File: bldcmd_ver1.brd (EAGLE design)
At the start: 43 x 49 mm, 94 parts, among them CN1 DF61-2P-2.2V(23), CN2 DF65-3P-1.7V(21), CN3 SM05B-SRSS-TB, CN5 SM04B-SRSS-TB, CN6 SM05B-SRSS-TB, CN7 SM04B-SRSS-TB, IC1 STSPIN32F0A, IC2 AS5047P-ATSM, IC3 ADM4852ACPZ-REEL7, Q1 PSMN2R4-30MLD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

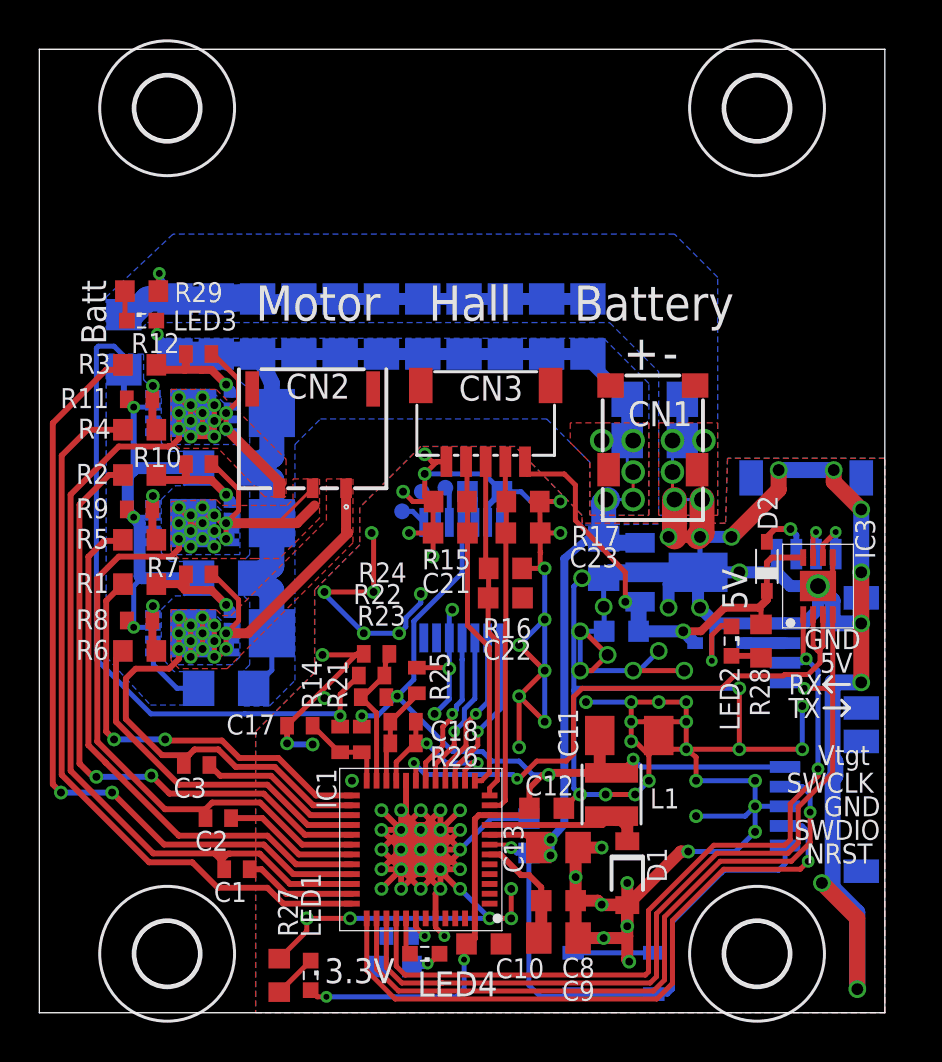
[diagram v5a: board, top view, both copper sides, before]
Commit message: RS485のICをSOIC8のものに変更
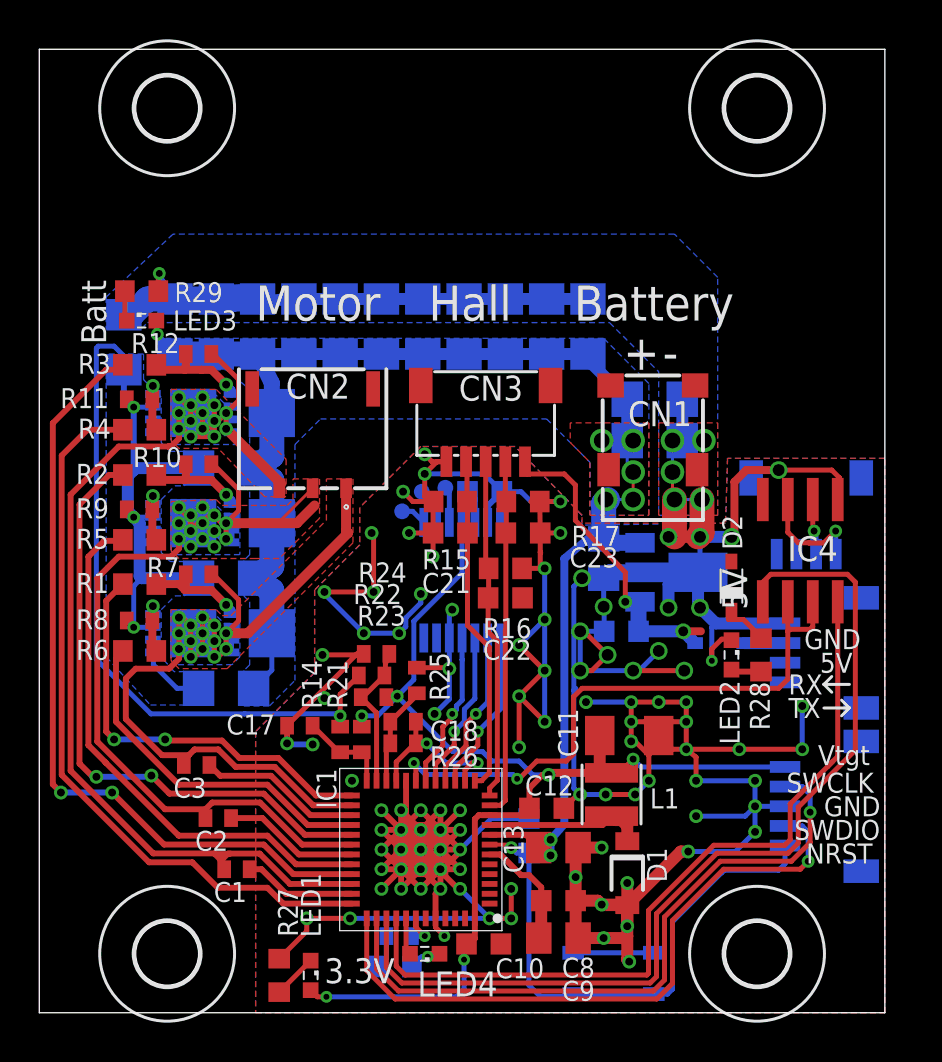
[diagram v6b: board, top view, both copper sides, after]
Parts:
- removed IC3: ADM4852ACPZ-REEL7, rcssl_lib:SON50P300X300X85-9N
- added IC4: LTC485S, linear-technology:SOIC8
- moved D2 2.06 mm to (35.2, 21.7)
- moved LED2 0.70 mm to (35.2, 18.2)
- moved R28 0.70 mm to (36.7, 18.2)
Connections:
- net +5V: now also IC4.8; no longer IC3.8
- net GND: now also IC4.5; no longer IC3.5, IC3.9
- net N$29: now also IC4.6; no longer IC3.7
- net N$32: now also IC4.7; no longer IC3.6
- net RTS: now also IC4.2, IC4.3; no longer IC3.2, IC3.3
- net UART_RX: now also IC1.39, IC4.1; no longer CN5.3, IC1.40, IC3.1
- net UART_TX: now also IC1.40, IC4.4; no longer CN5.4, IC1.39, IC3.4
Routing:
- net GND: track 382.9 -> 322.3 mm, vias 118 -> 108
- net UART_RX: track 40.8 -> 49.1 mm, vias 2 -> 0
- net +5V: track 25.9 -> 19.2 mm
- net UART_TX: track 44.3 -> 40.8 mm, vias 1 -> 0
- net N$32: track 2.69 -> 5.75 mm
- net N$30: track 3.01 -> 0.00 mm, vias 1 -> 0

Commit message: AW進捗
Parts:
- removed CN3: SM05B-SRSS-TB, scramble-con-jst:SM05B-SRSS-TB
- added CN4: DF57H-5P-1.2V(21), scramble-con-hirose:DF57H-5P-1.2V(21)
- C21, C22, C23: device rcl:C0603K -> rcl:C0402
- R15, R16, R17: device rcl:R0603 -> rcl:R0402
- moved R28 10.6 mm to (26.3, 20.2), turned to 0 degrees
- moved SW1 10.2 mm to (35.2, 10.3), flipped to the top
- moved LED2 9.56 mm to (26.3, 21.7), turned to 180 degrees
- moved R17 9.31 mm to (24.1, 16.7)
- moved R15 9.30 mm to (21.1, 16.7)
- moved C23 8.81 mm to (24.1, 15.6)
- moved C21 8.80 mm to (21.1, 15.6)
- moved R16 8.11 mm to (23.4, 14.5)
- moved C22 7.71 mm to (23.4, 13.4)
- moved IC4 6.00 mm to (38.7, 17.5)
- moved C9 1.94 mm to (24.8, 4.90)
- moved C8 1.84 mm to (24.8, 6.60)
- moved LED1 1.74 mm to (13.4, 3.60)
- moved R27 1.71 mm to (12.0, 3.60)
- moved D1 1.64 mm to (28.9, 8.40), turned to 180 degrees
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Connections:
- net +5V: now also CN4.1, LED2.A; no longer CN3.1, R28.2
- net GND: now also CN4.5, R28.1; no longer CN3.5, LED2.C
- net N$21: now also LED2.C, R28.2; no longer LED2.A, R28.1
- net N$23: now also CN4.4; no longer CN3.4
- net N$24: now also CN4.3; no longer CN3.3
- net N$25: now also CN4.2; no longer CN3.2
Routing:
- net N$24: track 17.4 -> 12.3 mm
- net GND: track 322.3 -> 317.1 mm, vias 108 -> 80
- net UART_TX: track 40.8 -> 35.7 mm
- net NRST: track 28.5 -> 23.3 mm, vias 1 -> 2
- net N$23: track 17.2 -> 12.2 mm
- net +3V3: track 64.6 -> 69.3 mm, vias 6 -> 5
- net N$25: track 18.3 -> 13.7 mm
- net N$30: track 0.00 -> 4.44 mm, vias 0 -> 1
- net UART_RX: track 49.1 -> 44.7 mm
- net RTS: track 30.6 -> 27.3 mm, vias 2 -> 4
- net N$29: track 2.84 -> 5.22 mm
- net N$18: track 8.17 -> 9.69 mm
- net LS_U: track 37.4 -> 36.1 mm
- net HS_W: track 21.7 -> 20.4 mm
- net HS_U: track 40.4 -> 39.1 mm
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
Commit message: AW進捗
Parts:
- moved C20 5.15 mm to (28.0, 18.0), turned to 90 degrees
- moved C19 4.93 mm to (34.3, 17.9), turned to 90 degrees
- moved U$6 3.74 mm to (31.3, 18.8), turned to 0 degrees
- moved D2 2.52 mm to (37.7, 22.7), turned to 0 degrees
- moved D3 2.06 mm to (35.4, 20.7), turned to 270 degrees
- moved CN6 0.60 mm to (40.2, 11.1)
- moved CN5 0.60 mm to (40.2, 18.9)
- moved CN7 0.60 mm to (39.0, 26.2)
- renumbered CN4 to CN3
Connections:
- net UART_RX: now also CN5.3
- net UART_TX: now also CN5.4
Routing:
- net UART_TX: track 35.7 -> 41.3 mm, vias 0 -> 1
- net UART_RX: track 44.7 -> 48.2 mm, vias 0 -> 1
- net +5V: track 19.7 -> 23.0 mm
- net GND: track 317.1 -> 314.3 mm
- net N$30: track 4.44 -> 2.38 mm
- net +12V: track 78.5 -> 79.6 mm
- net N$32: track 5.05 -> 5.65 mm
- net SWDIO: track 34.5 -> 35.1 mm
- net SWCLK: track 35.2 -> 35.8 mm
